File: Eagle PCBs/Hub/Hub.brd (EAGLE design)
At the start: 110.2 x 47 mm, 10 parts

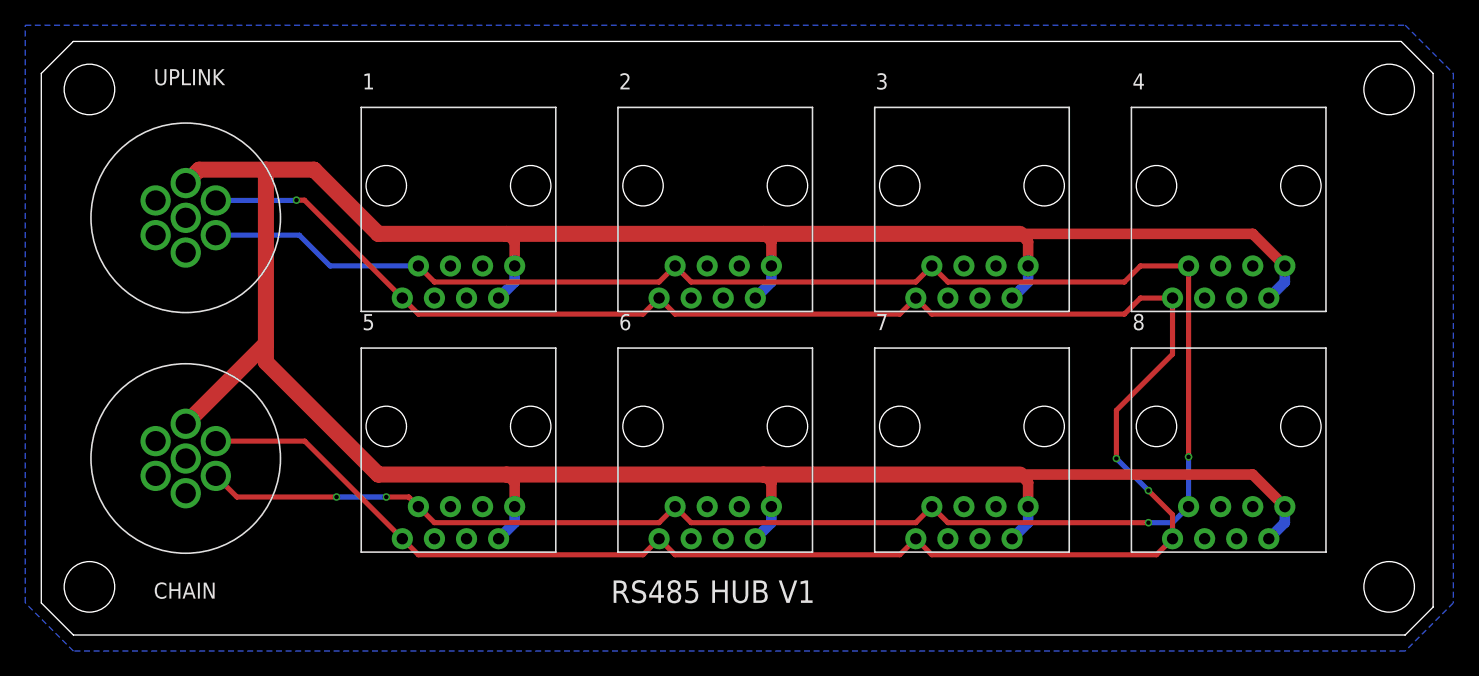
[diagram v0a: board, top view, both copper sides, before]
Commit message: Added a 5v bus to all PCBs
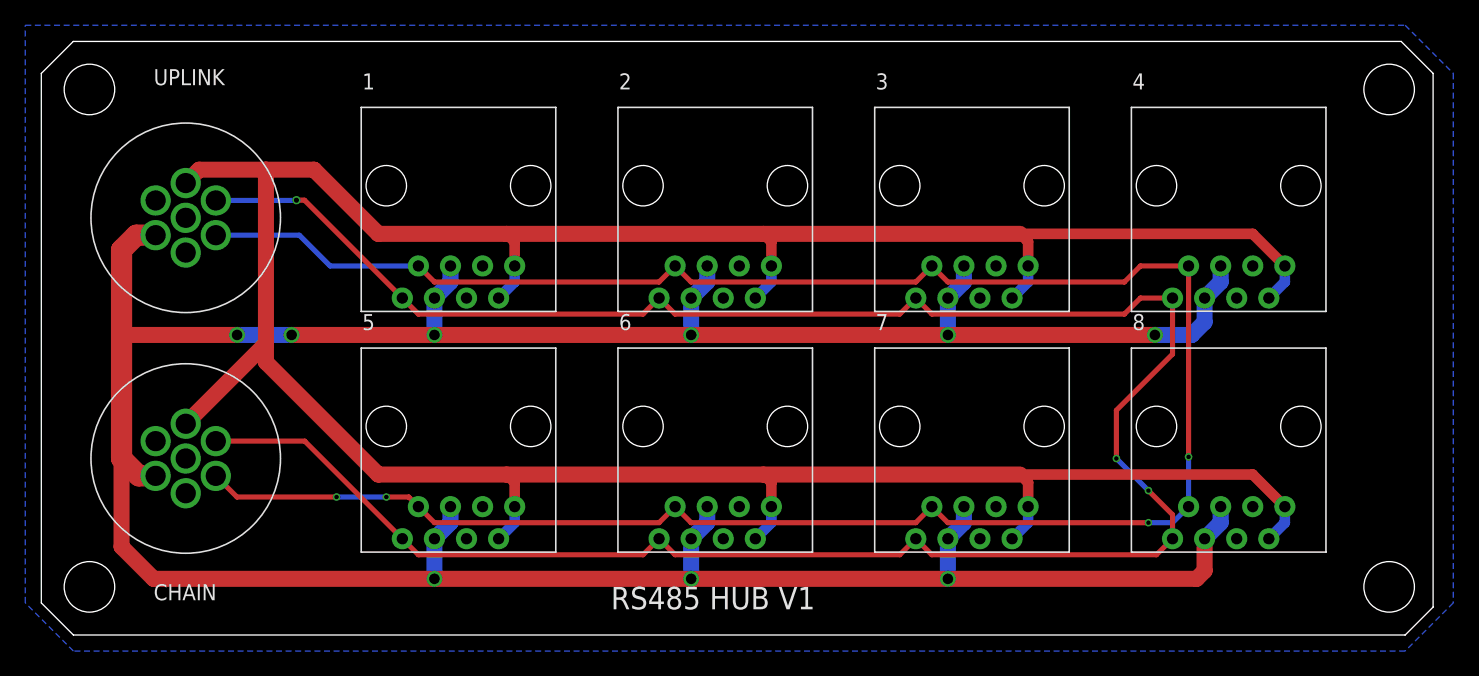
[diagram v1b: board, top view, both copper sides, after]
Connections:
- new net 5VCC: 1.5, 1.6, 2.5, 2.6, 3.5, 3.6, 4.5, 4.6, 5.5, 5.6, 6.5, 6.6, 7.5, 7.6, 8.5, 8.6, CHAIN.5, UPLINK.5
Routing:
- net 5VCC: track 0.00 -> 250.4 mm, vias 0 -> 9
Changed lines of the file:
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@@
 <hole x="106.68" y="43.18" drill="4"/>
 <hole x="106.68" y="3.81" drill="4"/>
-<text x="45.085" y="2.54" size="1.778" layer="25">RS485 HUB V1</text>
+<text x="45.085" y="2.032" size="1.778" layer="25">RS485 HUB V1</text>
 <text x="109.22" y="26.67" size="7.62" layer="26" rot="MR355">BRRRRRRRRRRRRT</text>
 </plain>
@@
 <class number="0" name="default" width="0.4064" drill="0.254">
 <clearance class="0" value="0.1524"/>
+</class>
+<class number="1" name="5VCC" width="0.8382" drill="0.5334">
+<clearance class="1" value="0.1524"/>
 </class>
 </classes>
@@
 </element>
 <element name="CHAIN" library="A10 Library" package="GX12-7P" value="GX12-7P" x="11.43" y="13.97" smashed="yes">
-<attribute name="NAME" x="8.89" y="2.877" size="1.27" layer="25" ratio="10"/>
+<attribute name="NAME" x="8.89" y="2.75" size="1.27" layer="25" ratio="10"/>
 </element>
 <element name="UPLINK" library="A10 Library" package="GX12-7P" value="GX12-7P" x="11.43" y="33.02" smashed="yes">
@@
 <wire x1="28.575" y1="7.62" x2="20.85" y2="15.345" width="0.4064" layer="1"/>
 <wire x1="20.85" y1="15.345" x2="13.8115" y2="15.345" width="0.4064" layer="1"/>
-<wire x1="13.8115" y1="34.395" x2="20.215" y2="34.395" width="0.4064" layer="16"/>
-<via x="20.193" y="34.417" extent="1-16" drill="0.35"/>
 <wire x1="20.193" y1="34.417" x2="20.828" y2="34.417" width="0.4064" layer="1"/>
-<wire x1="20.828" y1="34.417" x2="28.575" y2="26.67" width="0.4064" layer="1"/>
-<wire x1="20.193" y1="34.417" x2="20.215" y2="34.395" width="0" layer="19" extent="16-16"/>
+<wire x1="28.575" y1="26.67" x2="20.828" y2="34.417" width="0.4064" layer="1"/>
+<via x="20.193" y="34.417" extent="1-16" drill="0.4064"/>
+<wire x1="13.8115" y1="34.395" x2="20.171" y2="34.395" width="0.4064" layer="16"/>
+<wire x1="20.171" y1="34.395" x2="20.193" y2="34.417" width="0.4064" layer="16"/>
 </signal>
 <signal name="B">
@@
 <wire x1="86.995" y1="29.21" x2="90.805" y2="29.21" width="0.4064" layer="1"/>
 <wire x1="71.755" y1="27.94" x2="85.725" y2="27.94" width="0.4064" layer="1"/>
-<wire x1="90.805" y1="29.21" x2="90.805" y2="14.1097" width="0.4064" layer="1"/>
 <via x="90.805" y="14.097" extent="1-16" drill="0.35"/>
 <wire x1="90.805" y1="14.097" x2="90.805" y2="10.16" width="0.4064" layer="16"/>
@@
 <wire x1="23.368" y1="10.922" x2="15.4845" y2="10.922" width="0.4064" layer="1"/>
 <wire x1="15.4845" y1="10.922" x2="13.8115" y2="12.595" width="0.4064" layer="1"/>
-<wire x1="90.805" y1="14.097" x2="90.805" y2="14.1097" width="0" layer="19" extent="1-1"/>
+<wire x1="90.805" y1="14.097" x2="90.805" y2="29.21" width="0.4064" layer="1"/>
 </signal>
 <signal name="GND">
@@
 <contactref element="5" pad="4"/>
 </signal>
+<signal name="5VCC" class="1">
+<contactref element="UPLINK" pad="5"/>
+<contactref element="CHAIN" pad="5"/>
+<contactref element="1" pad="5"/>
+<contactref element="1" pad="6"/>
+<contactref element="2" pad="5"/>
+<contactref element="3" pad="5"/>
+<contactref element="4" pad="5"/>
+<contactref element="6" pad="5"/>
+<contactref element="5" pad="5"/>
+<contactref element="7" pad="5"/>
+<contactref element="8" pad="5"/>
+<contactref element="2" pad="6"/>
+<contactref element="5" pad="6"/>
+<contactref element="6" pad="6"/>
+<contactref element="3" pad="6"/>
+<contactref element="4" pad="6"/>
+<contactref element="8" pad="6"/>
+<contactref element="7" pad="6"/>
+<wire x1="9.0485" y1="31.645" x2="7.515" y2="31.645" width="1.6764" layer="1"/>
+<wire x1="7.515" y1="31.645" x2="6.35" y2="30.48" width="1.6764" layer="1"/>
+<wire x1="6.35" y1="30.48" x2="6.35" y2="23.749" width="1.6764" layer="1"/>
+<wire x1="6.35" y1="23.749" x2="6.35" y2="13.97" width="1.6764" layer="1"/>
+<wire x1="6.35" y1="13.97" x2="7.725" y2="12.595" width="1.6764" layer="1"/>
+<wire x1="9.0485" y1="12.595" x2="7.725" y2="12.595" width="1.6764" layer="1"/>
+<wire x1="31.115" y1="26.67" x2="31.115" y2="23.749" width="1.27" layer="16"/>
+<via x="31.115" y="23.749" extent="1-16" drill="0.8382"/>
+<wire x1="31.115" y1="23.749" x2="19.812" y2="23.749" width="1.27" layer="1"/>
+<via x="19.812" y="23.749" extent="1-16" drill="0.8382"/>
+<wire x1="19.812" y1="23.749" x2="15.494" y2="23.749" width="1.27" layer="16"/>
+<via x="15.494" y="23.749" extent="1-16" drill="0.8382"/>
+<wire x1="15.494" y1="23.749" x2="6.35" y2="23.749" width="1.27" layer="1"/>
+<wire x1="31.115" y1="23.749" x2="51.435" y2="23.749" width="1.27" layer="1"/>
+<wire x1="51.435" y1="23.749" x2="71.755" y2="23.749" width="1.27" layer="1"/>
+<via x="51.435" y="23.749" extent="1-16" drill="0.8382"/>
+<via x="71.755" y="23.749" extent="1-16" drill="0.8382"/>
+<wire x1="71.755" y1="26.67" x2="71.755" y2="23.749" width="1.27" layer="16"/>
+<wire x1="51.435" y1="26.67" x2="51.435" y2="23.749" width="1.27" layer="16"/>
+<wire x1="71.755" y1="23.749" x2="88.138" y2="23.749" width="1.27" layer="1"/>
+<via x="88.138" y="23.749" extent="1-16" drill="0.8382"/>
+<wire x1="88.138" y1="23.749" x2="91.059" y2="23.749" width="1.27" layer="16"/>
+<wire x1="91.059" y1="23.749" x2="92.075" y2="24.765" width="1.27" layer="16"/>
+<wire x1="92.075" y1="24.765" x2="92.075" y2="26.67" width="1.27" layer="16"/>
+<wire x1="6.35" y1="13.97" x2="6.35" y2="6.985" width="1.27" layer="1"/>
+<wire x1="6.35" y1="6.985" x2="8.89" y2="4.445" width="1.27" layer="1"/>
+<wire x1="8.89" y1="4.445" x2="31.115" y2="4.445" width="1.27" layer="1"/>
+<wire x1="31.115" y1="4.445" x2="51.435" y2="4.445" width="1.27" layer="1"/>
+<wire x1="51.435" y1="4.445" x2="71.755" y2="4.445" width="1.27" layer="1"/>
+<wire x1="92.075" y1="7.62" x2="92.075" y2="5.08" width="1.27" layer="1"/>
+<wire x1="92.075" y1="5.08" x2="91.44" y2="4.445" width="1.27" layer="1"/>
+<wire x1="91.44" y1="4.445" x2="71.755" y2="4.445" width="1.27" layer="1"/>
+<wire x1="31.115" y1="26.67" x2="32.385" y2="27.94" width="1.27" layer="16"/>
+<wire x1="32.385" y1="27.94" x2="32.385" y2="29.21" width="1.27" layer="16"/>
+<wire x1="51.435" y1="26.67" x2="52.705" y2="27.94" width="1.27" layer="16"/>
+<wire x1="52.705" y1="27.94" x2="52.705" y2="29.21" width="1.27" layer="16"/>
+<wire x1="71.755" y1="26.67" x2="73.025" y2="27.94" width="1.27" layer="16"/>
+<wire x1="73.025" y1="27.94" x2="73.025" y2="29.21" width="1.27" layer="16"/>
+<wire x1="92.075" y1="26.67" x2="93.345" y2="27.94" width="1.27" layer="16"/>
+<wire x1="93.345" y1="27.94" x2="93.345" y2="29.21" width="1.27" layer="16"/>
+<wire x1="92.075" y1="7.62" x2="93.345" y2="8.89" width="1.27" layer="16"/>
+<wire x1="93.345" y1="8.89" x2="93.345" y2="10.16" width="1.27" layer="16"/>
+<wire x1="71.755" y1="7.62" x2="73.025" y2="8.89" width="1.27" layer="16"/>
+<wire x1="73.025" y1="8.89" x2="73.025" y2="10.16" width="1.27" layer="16"/>
+<wire x1="51.435" y1="7.62" x2="52.705" y2="8.89" width="1.27" layer="16"/>
+<wire x1="52.705" y1="8.89" x2="52.705" y2="10.16" width="1.27" layer="16"/>
+<wire x1="31.115" y1="7.62" x2="32.385" y2="8.89" width="1.27" layer="16"/>
+<wire x1="32.385" y1="8.89" x2="32.385" y2="10.16" width="1.27" layer="16"/>
+<via x="31.115" y="4.445" extent="1-16" drill="0.8382"/>
+<via x="51.435" y="4.445" extent="1-16" drill="0.8382"/>
+<via x="71.755" y="4.445" extent="1-16" drill="0.8382"/>
+<wire x1="71.755" y1="7.62" x2="71.755" y2="4.445" width="1.27" layer="16"/>
+<wire x1="51.435" y1="7.62" x2="51.435" y2="4.445" width="1.27" layer="16"/>
+<wire x1="31.115" y1="7.62" x2="31.115" y2="4.445" width="1.27" layer="16"/>
+</signal>
 </signals>
